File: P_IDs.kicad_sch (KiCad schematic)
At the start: 0 parts

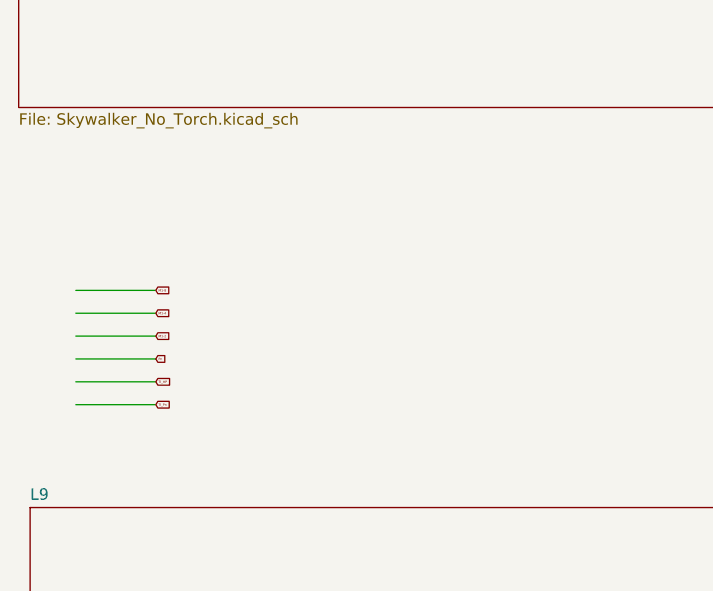
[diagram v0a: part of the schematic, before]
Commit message: added universal key
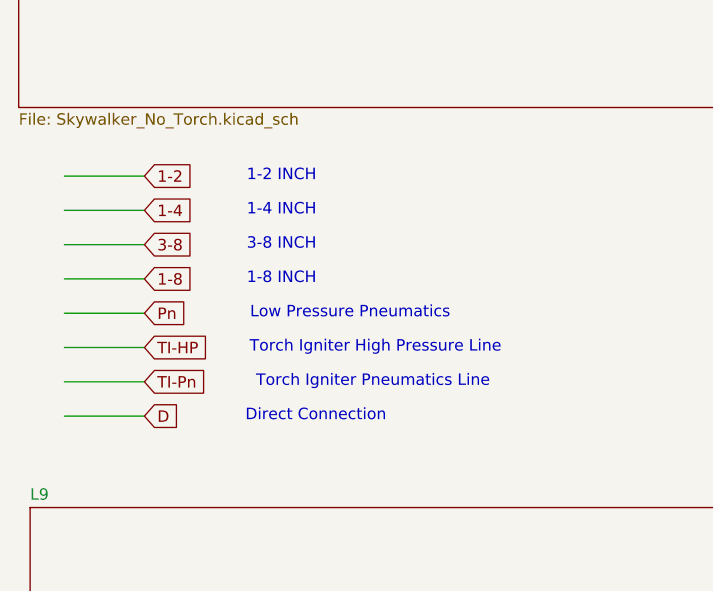
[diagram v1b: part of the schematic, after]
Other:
- note added: "1-2 INCH"
- note added: "1-4 INCH"
- note added: "1-8 INCH"
- note added: "3-8 INCH"
- note added: "Direct Connection"
- note added: "Low Pressure Pneumatics"
- note added: "Torch Igniter High Pressure Line"
- note added: "Torch Igniter Pneumatics Line"
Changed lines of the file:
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@@
 	(generator_version "9.0")
 	(paper "A4")
-	(wire
-		(pts
-			(xy 22.86 87.63) (xy 31.75 87.63)
-		)
-		(stroke
-			(width 0)
-			(type default)
-		)
-	)
-	(wire
-		(pts
-			(xy 22.86 85.09) (xy 31.75 85.09)
-		)
-		(stroke
-			(width 0)
-			(type default)
-		)
-	)
-	(wire
-		(pts
-			(xy 22.86 92.71) (xy 31.75 92.71)
-		)
-		(stroke
-			(width 0)
-			(type default)
-		)
-	)
-	(wire
-		(pts
-			(xy 22.86 82.55) (xy 31.75 82.55)
-		)
-		(stroke
-			(width 0)
-			(type default)
-		)
-	)
-	(wire
-		(pts
-			(xy 22.86 90.17) (xy 31.75 90.17)
-		)
-		(stroke
-			(width 0)
-			(type default)
-		)
-	)
-	(wire
-		(pts
-			(xy 22.86 95.25) (xy 31.75 95.25)
-		)
-		(stroke
-			(width 0)
-			(type default)
-		)
-	)
-	(global_label "M1-4"
-		(shape input)
-		(at 31.75 85.09 0)
-		(fields_autoplaced yes)
-		(effects
-			(font
-				(size 0.254 0.254)
-			)
-			(justify left)
-		)
-		(property "Intersheetrefs" "${INTERSHEET_REFS}"
-			(at 33.4362 85.09 0)
+	(text " Torch Igniter High Pressure Line"
+		(exclude_from_sim no)
+		(at 55.88 88.9 0)
+		(effects
+			(font
+				(size 1.27 1.27)
+			)
+		)
+	)
+	(text "1-2 INCH\n"
+		(exclude_from_sim no)
+		(at 45.72 69.85 0)
+		(effects
+			(font
+				(size 1.27 1.27)
+			)
+		)
+	)
+	(text "Low Pressure Pneumatics"
+		(exclude_from_sim no)
+		(at 53.34 85.09 0)
+		(effects
+			(font
+				(size 1.27 1.27)
+			)
+		)
+	)
+	(text "1-4 INCH\n"
+		(exclude_from_sim no)
+		(at 45.72 73.66 0)
+		(effects
+			(font
+				(size 1.27 1.27)
+			)
+		)
+	)
+	(text "Torch Igniter Pneumatics Line"
+		(exclude_from_sim no)
+		(at 55.88 92.71 0)
+		(effects
+			(font
+				(size 1.27 1.27)
+			)
+		)
+	)
+	(text "3-8 INCH\n"
+		(exclude_from_sim no)
+		(at 45.72 77.47 0)
+		(effects
+			(font
+				(size 1.27 1.27)
+			)
+		)
+	)
+	(text "Direct Connection"
+		(exclude_from_sim no)
+		(at 49.53 96.52 0)
+		(effects
+			(font
+				(size 1.27 1.27)
+			)
+		)
+	)
+	(text "1-8 INCH\n"
+		(exclude_from_sim no)
+		(at 45.72 81.28 0)
+		(effects
+			(font
+				(size 1.27 1.27)
+			)
+		)
+	)
+	(wire
+		(pts
+			(xy 21.59 77.47) (xy 30.48 77.47)
+		)
+		(stroke
+			(width 0)
+			(type default)
+		)
+	)
+	(wire
+		(pts
+			(xy 21.59 85.09) (xy 30.48 85.09)
+		)
+		(stroke
+			(width 0)
+			(type default)
+		)
+	)
+	(wire
+		(pts
+			(xy 21.59 81.28) (xy 30.48 81.28)
+		)
+		(stroke
+			(width 0)
+			(type default)
+		)
+	)
+	(wire
+		(pts
+			(xy 21.59 69.85) (xy 30.48 69.85)
+		)
+		(stroke
+			(width 0)
+			(type default)
+		)
+	)
+	(wire
+		(pts
+			(xy 21.59 96.52) (xy 30.48 96.52)
+		)
+		(stroke
+			(width 0)
+			(type default)
+		)
+	)
+	(wire
+		(pts
+			(xy 21.59 88.9) (xy 30.48 88.9)
+		)
+		(stroke
+			(width 0)
+			(type default)
+		)
+	)
+	(wire
+		(pts
+			(xy 21.59 92.71) (xy 30.48 92.71)
+		)
+		(stroke
+			(width 0)
+			(type default)
+		)
+	)
+	(wire
+		(pts
+			(xy 21.59 73.66) (xy 30.48 73.66)
+		)
+		(stroke
+			(width 0)
+			(type default)
+		)
+	)
+	(global_label "1-8"
+		(shape input)
+		(at 30.48 81.28 0)
+		(fields_autoplaced yes)
+		(effects
+			(font
+				(size 1.27 1.27)
+			)
+			(justify left)
+		)
+		(property "Intersheetrefs" "${INTERSHEET_REFS}"
+			(at 37.4566 81.28 0)
 			(effects
 				(font
@@
 	(global_label "Pn"
 		(shape input)
-		(at 31.75 90.17 0)
-		(fields_autoplaced yes)
-		(effects
-			(font
-				(size 0.254 0.254)
-			)
-			(justify left)
-		)
-		(property "Intersheetrefs" "${INTERSHEET_REFS}"
-			(at 32.8314 90.17 0)
-			(effects
-				(font
-					(size 1.27 1.27)
-				)
-				(justify left)
-				(hide yes)
-			)
-		)
-	)
-	(global_label "M1-2"
-		(shape input)
-		(at 31.75 87.63 0)
-		(fields_autoplaced yes)
-		(effects
-			(font
-				(size 0.254 0.254)
-			)
-			(justify left)
-		)
-		(property "Intersheetrefs" "${INTERSHEET_REFS}"
-			(at 33.4362 87.63 0)
-			(effects
-				(font
-					(size 1.27 1.27)
-				)
-				(justify left)
-				(hide yes)
-			)
-		)
-	)
-	(global_label "M1-8"
-		(shape input)
-		(at 31.75 82.55 0)
-		(fields_autoplaced yes)
-		(effects
-			(font
-				(size 0.254 0.254)
-			)
-			(justify left)
-		)
-		(property "Intersheetrefs" "${INTERSHEET_REFS}"
-			(at 33.4362 82.55 0)
-			(effects
-				(font
-					(size 1.27 1.27)
-				)
-				(justify left)
-				(hide yes)
-			)
-		)
-	)
-	(global_label "TI_HP"
-		(shape input)
-		(at 31.75 92.71 0)
-		(fields_autoplaced yes)
-		(effects
-			(font
-				(size 0.254 0.254)
-			)
-			(justify left)
-		)
-		(property "Intersheetrefs" "${INTERSHEET_REFS}"
-			(at 33.3757 92.71 0)
-			(effects
-				(font
-					(size 1.27 1.27)
-				)
-				(justify left)
-				(hide yes)
-			)
-		)
-	)
-	(global_label "TI_Pn"
-		(shape input)
-		(at 31.75 95.25 0)
-		(fields_autoplaced yes)
-		(effects
-			(font
-				(size 0.254 0.254)
-			)
-			(justify left)
-		)
-		(property "Intersheetrefs" "${INTERSHEET_REFS}"
-			(at 33.3394 95.25 0)
-			(effects
-				(font
+		(at 30.48 85.09 0)
+		(fields_autoplaced yes)
+		(effects
+			(font
+				(size 1.27 1.27)
+			)
+			(justify left)
+		)
+		(property "Intersheetrefs" "${INTERSHEET_REFS}"
+			(at 35.8842 85.09 0)
+			(effects
+				(font
+					(size 1.27 1.27)
+				)
+				(justify left)
+				(hide yes)
+			)
+		)
+	)
+	(global_label "TI-HP"
+		(shape input)
+		(at 30.48 88.9 0)
+		(fields_autoplaced yes)
+		(effects
+			(font
+				(size 1.27 1.27)
+			)
+			(justify left)
+		)
+		(property "Intersheetrefs" "${INTERSHEET_REFS}"
+			(at 39.2105 88.9 0)
+			(effects
+				(font
+					(size 1.27 1.27)
+				)
+				(justify left)
+				(hide yes)
+			)
+		)
+	)
+	(global_label "3-8"
+		(shape input)
+		(at 30.48 77.47 0)
+		(fields_autoplaced yes)
+		(effects
+			(font
+				(size 1.27 1.27)
+			)
+			(justify left)
+		)
+		(property "Intersheetrefs" "${INTERSHEET_REFS}"
+			(at 37.4566 77.47 0)
+			(effects
+				(font
+					(size 1.27 1.27)
+				)
+				(justify left)
+				(hide yes)
+			)
+		)
+	)
+	(global_label "TI-Pn"
+		(shape input)
+		(at 30.48 92.71 0)
+		(fields_autoplaced yes)
+		(effects
+			(font
+				(size 1.27 1.27)
+			)
+			(justify left)
+		)
+		(property "Intersheetrefs" "${INTERSHEET_REFS}"
+			(at 39.029 92.71 0)
+			(effects
+				(font
+					(size 1.27 1.27)
+				)
+				(justify left)
+				(hide yes)
+			)
+		)
+	)
+	(global_label "D"
+		(shape input)
+		(at 30.48 96.52 0)
+		(fields_autoplaced yes)
+		(effects
+			(font
+				(size 1.27 1.27)
+			)
+			(justify left)
+		)
+		(property "Intersheetrefs" "${INTERSHEET_REFS}"
+			(at 34.7352 96.52 0)
+			(effects
+				(font
+					(size 1.27 1.27)
+				)
+				(justify left)
+				(hide yes)
+			)
+		)
+	)
+	(global_label "1-4"
+		(shape input)
+		(at 30.48 73.66 0)
+		(fields_autoplaced yes)
+		(effects
+			(font
+				(size 1.27 1.27)
+			)
+			(justify left)
+		)
+		(property "Intersheetrefs" "${INTERSHEET_REFS}"
+			(at 37.4566 73.66 0)
+			(effects
+				(font
+					(size 1.27 1.27)
+				)
+				(justify left)
+				(hide yes)
+			)
+		)
+	)
+	(global_label "1-2"
+		(shape input)
+		(at 30.48 69.85 0)
+		(fields_autoplaced yes)
+		(effects
+			(font
+				(size 1.27 1.27)
+			)
+			(justify left)
+		)
+		(property "Intersheetrefs" "${INTERSHEET_REFS}"
+			(at 37.4566 69.85 0)
+			(effects
+				(font

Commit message: Small visual changes
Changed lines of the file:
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@@
 	)
 	(sheet
-		(at 85.09 161.29)
-		(size 73.66 26.67)
+		(at 127 106.68)
+		(size 105.41 46.99)
 		(exclude_from_sim no)
 		(in_bom yes)
@@
 		)
 		(property "Sheetname" "Pluto GSS"
-			(at 85.09 160.5784 0)
+			(at 127 105.9684 0)
 			(effects
 				(font
@@
 		)
 		(property "Sheetfile" "Pluto_GSS.kicad_sch"
-			(at 85.09 188.5446 0)
+			(at 127 154.2546 0)
 			(effects
 				(font
@@
 	)
 	(sheet
-		(at 17.78 160.02)
-		(size 57.15 27.94)
+		(at 17.78 134.62)
+		(size 102.87 20.32)
 		(exclude_from_sim no)
 		(in_bom yes)
@@
 		)
 		(property "Sheetname" "Pluto Common Dome"
-			(at 17.78 159.3084 0)
+			(at 17.78 133.9084 0)
 			(effects
 				(font
@@
 		)
 		(property "Sheetfile" "Pluto_Common_Dome.kicad_sch"
-			(at 17.78 188.5446 0)
+			(at 17.78 155.5246 0)
 			(effects
 				(font
@@
 	(sheet
 		(at 17.78 106.68)
-		(size 215.9 45.72)
+		(size 102.87 22.86)
 		(exclude_from_sim no)
 		(in_bom yes)
@@
 		)
 		(property "Sheetfile" "L9.kicad_sch"
-			(at 17.78 152.9846 0)
+			(at 17.78 130.1246 0)
 			(effects
 				(font

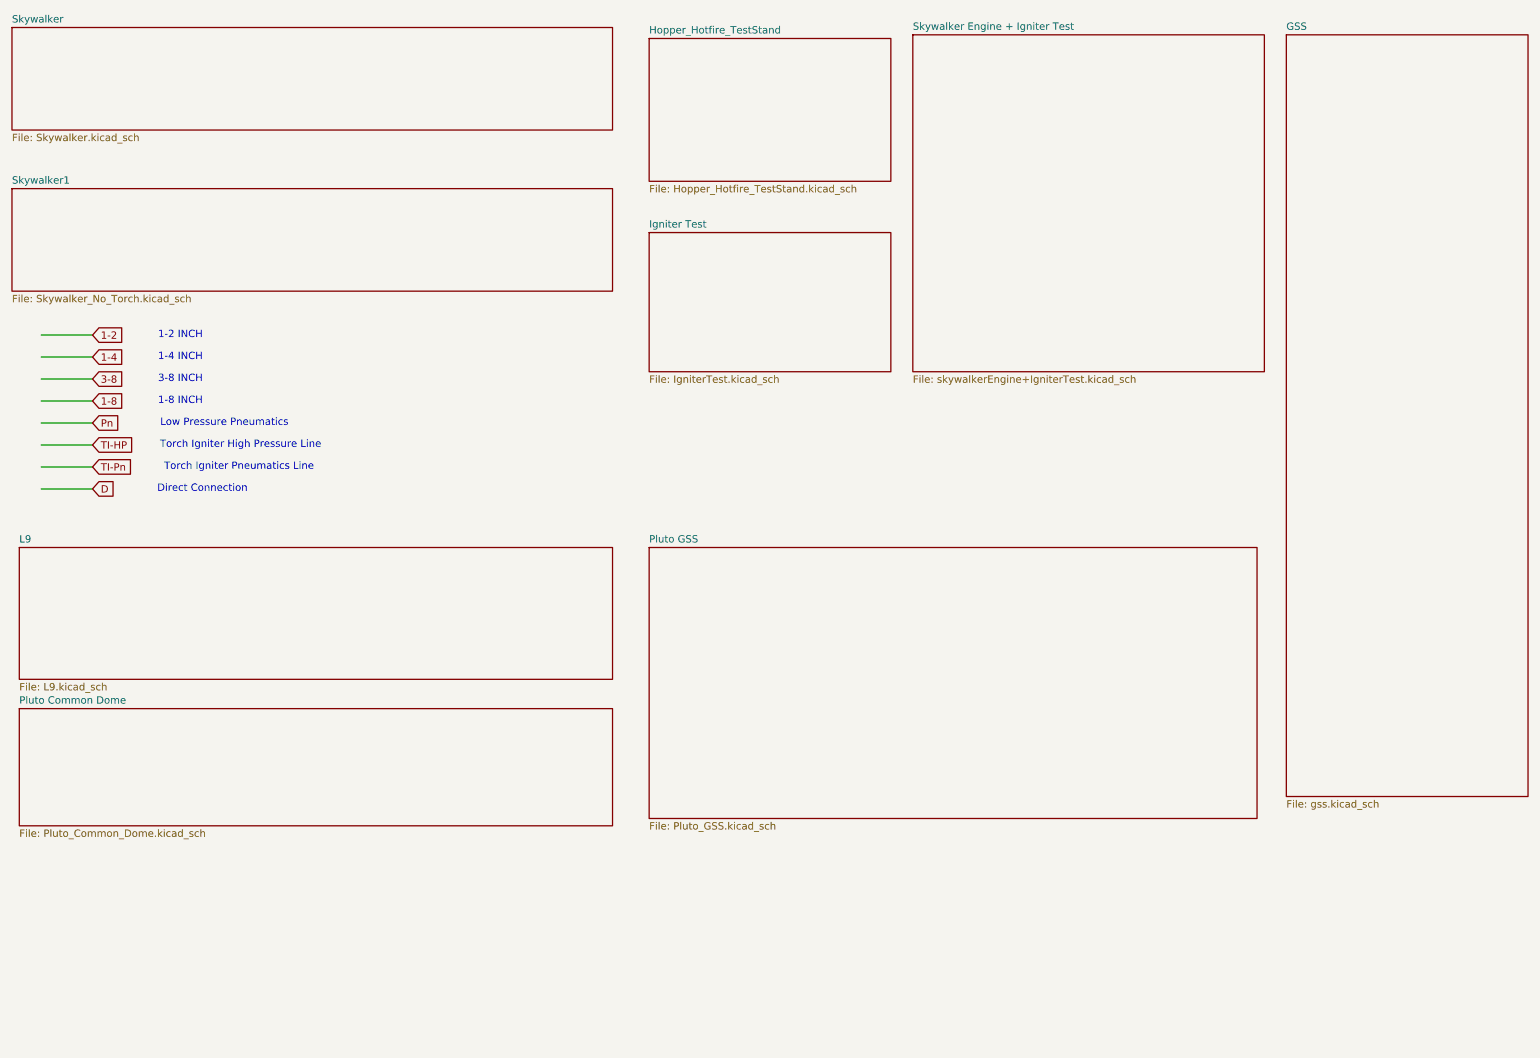
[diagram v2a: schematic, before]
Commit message: cleanup cos i was bored and procastinating. mini tutorial on defining pipe sizes in the p&id.
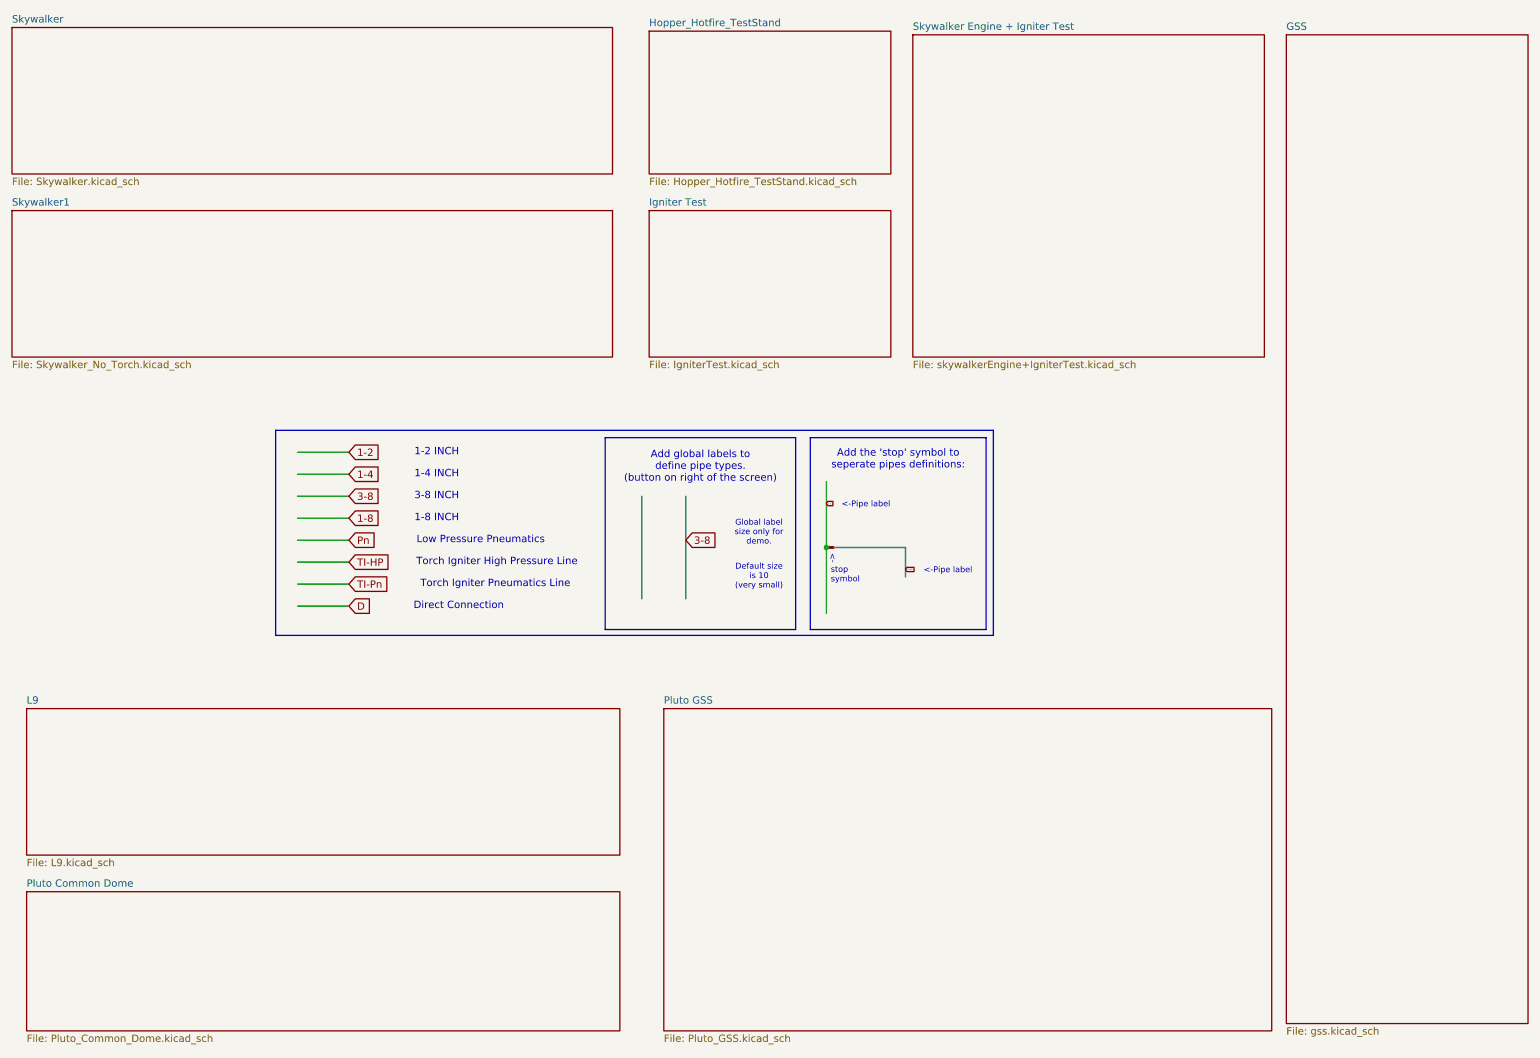
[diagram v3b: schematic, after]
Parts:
- added U6: ~, symbol PID_symbols:stop
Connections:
- net 1-2: now also U6.
- net TI-HP: now also U6.
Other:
- note added: "->"
- note added: "<-Pipe label"
- note added: "Add global labels to define pipe types. (button on right of the screen)"
- note added: "Add the 'stop' symbol to seperate pipes definitions:"
- note added: "Default size is 10 (very small)"
- note added: "Global label size only for demo."
- note added: "stop symbol"
